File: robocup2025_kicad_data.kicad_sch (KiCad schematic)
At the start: 13 parts, among them M7 Motor_Servo, U2 ESP32-DEVKITC-32E

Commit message: added switch
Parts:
- added S1: tactile switch, robo:tactile switch, symbol robo:tactile switch
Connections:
- net ESP32_3.3: now also S1.2
- net ESP32_21: now reaches U2.J3_6 (IO21)
- net ESP32_21: now also S1.1
- no-connect marks 25 -> 24

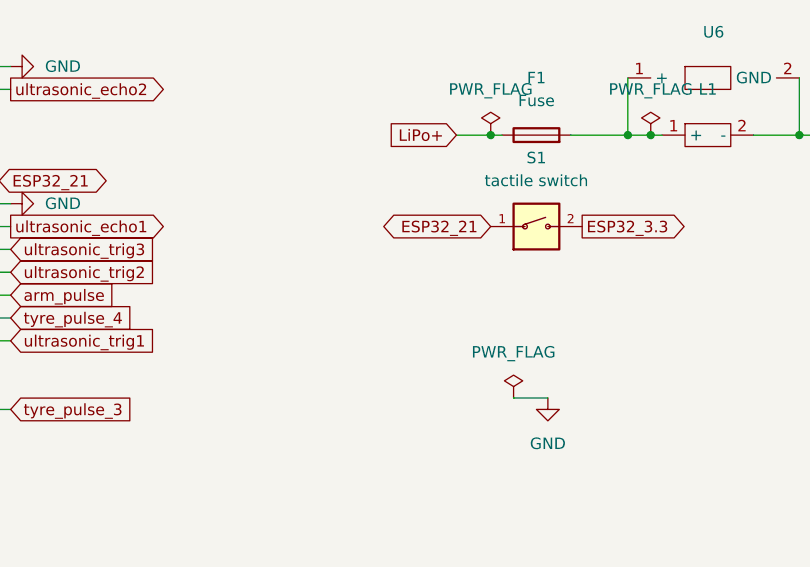
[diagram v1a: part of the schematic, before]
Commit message: fix: Made the pin "non-floating"
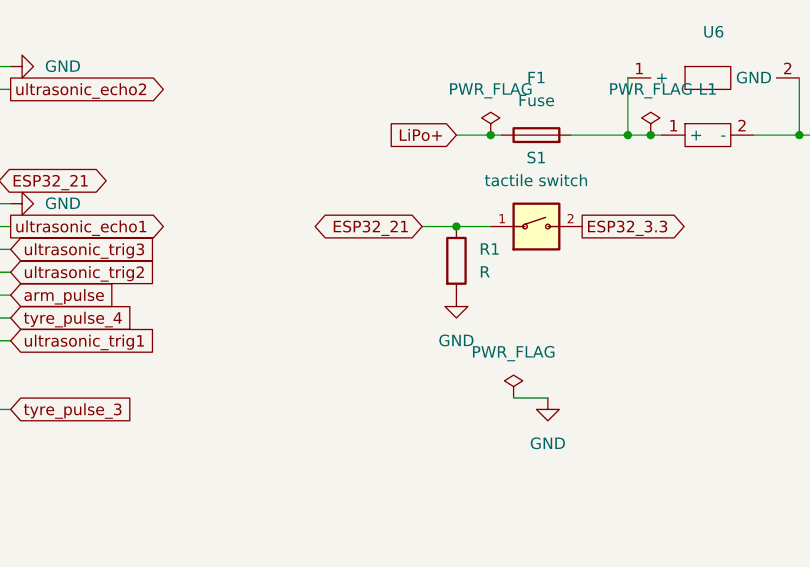
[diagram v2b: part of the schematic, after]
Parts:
- added R1: R, symbol Device:R
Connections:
- net ESP32_21: now also R1.1
- net GND: now also R1.2
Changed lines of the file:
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@@
 	)
 	(junction
+		(at 135.89 48.26)
+		(diameter 0)
+		(color 0 0 0 0)
+	)
+	(junction
 		(at 157.48 38.1)
 		(diameter 0)
@@
 	(wire
 		(pts
+			(xy 135.89 48.26) (xy 139.7 48.26)
+		)
+		(stroke
+			(width 0)
+			(type default)
+		)
+	)
+	(wire
+		(pts
 			(xy 82.55 55.88) (xy 86.36 55.88)
 		)
@@
 	(wire
 		(pts
+			(xy 132.08 48.26) (xy 135.89 48.26)
+		)
+		(stroke
+			(width 0)
+			(type default)
+		)
+	)
+	(wire
+		(pts
 			(xy 133.35 120.65) (xy 133.35 124.46)
 		)
@@
 	(global_label "ESP32_21"
 		(shape bidirectional)
-		(at 139.7 48.26 180)
+		(at 132.08 48.26 180)
 		(fields_autoplaced yes)
 		(effects
@@
 		)
 		(property "Intersheetrefs" "${INTERSHEET_REFS}"
-			(at 126.1694 48.26 0)
+			(at 118.5494 48.26 0)
 			(effects
 				(font
@@
 	)
 	(symbol
+		(lib_id "power:GND")
+		(at 135.89 55.88 0)
+		(unit 1)
+		(exclude_from_sim no)
+		(in_bom yes)
+		(on_board yes)
+		(dnp no)
+		(fields_autoplaced yes)
+		(property "Reference" "#PWR05"
+			(at 135.89 62.23 0)
+			(effects
+				(font
+					(size 1.27 1.27)
+				)
+				(hide yes)
+			)
+		)
+		(property "Value" "GND"
+			(at 135.89 60.96 0)
+			(effects
+				(font
+					(size 1.27 1.27)
+				)
+			)
+		)
+		(property "Footprint" ""
+			(at 135.89 55.88 0)
+			(effects
+				(font
+					(size 1.27 1.27)
+				)
+				(hide yes)
+			)
+		)
+		(property "Datasheet" ""
+			(at 135.89 55.88 0)
+			(effects
+				(font
+					(size 1.27 1.27)
+				)
+				(hide yes)
+			)
+		)
+		(property "Description" "Power symbol creates a global label with name \"GND\" , ground"
+			(at 135.89 55.88 0)
+			(effects
+				(font
+					(size 1.27 1.27)
+				)
+				(hide yes)
+			)
+		)
+		(pin "1"
+		)
+		(instances
+			(project ""
+				(path "/c41ae4e6-c818-4751-9662-d6273ae109e5"
+					(reference "#PWR05")
+					(unit 1)
+				)
+			)
+		)
+	)
+	(symbol
 		(lib_id "power:PWR_FLAG")
 		(at 139.7 38.1 0)
@@
 					(unit 1)
 				)
+			)
+		)
+	)
+	(symbol
+		(lib_id "Device:R")
+		(at 135.89 52.07 0)
+		(unit 1)
+		(exclude_from_sim no)
+		(in_bom yes)
+		(on_board yes)
+		(dnp no)
+		(fields_autoplaced yes)
+		(property "Reference" "R1"
+			(at 138.43 50.7999 0)
+			(effects
+				(font
+					(size 1.27 1.27)
+				)
+				(justify left)
+			)
+		)
+		(property "Value" "R"
+			(at 138.43 53.3399 0)
+			(effects
+				(font
+					(size 1.27 1.27)
+				)
+				(justify left)
+			)
+		)
+		(property "Footprint" ""
+			(at 134.112 52.07 90)
+			(effects
+				(font
+					(size 1.27 1.27)
+				)
+				(hide yes)
+			)
+		)
+		(property "Datasheet" "~"
+			(at 135.89 52.07 0)
+			(effects
+				(font
+					(size 1.27 1.27)
+				)
+				(hide yes)
+			)
+		)
+		(property "Description" "Resistor"
+			(at 135.89 52.07 0)
+			(effects
+				(font
+					(size 1.27 1.27)
+				)
+				(hide yes)
+			)
+		)
+		(pin "2"
+		)
+		(pin "1"
+		)
+		(instances
+			(project ""
+				(path "/c41ae4e6-c818-4751-9662-d6273ae109e5"
+					(reference "R1")
+					(unit 1)
+				)

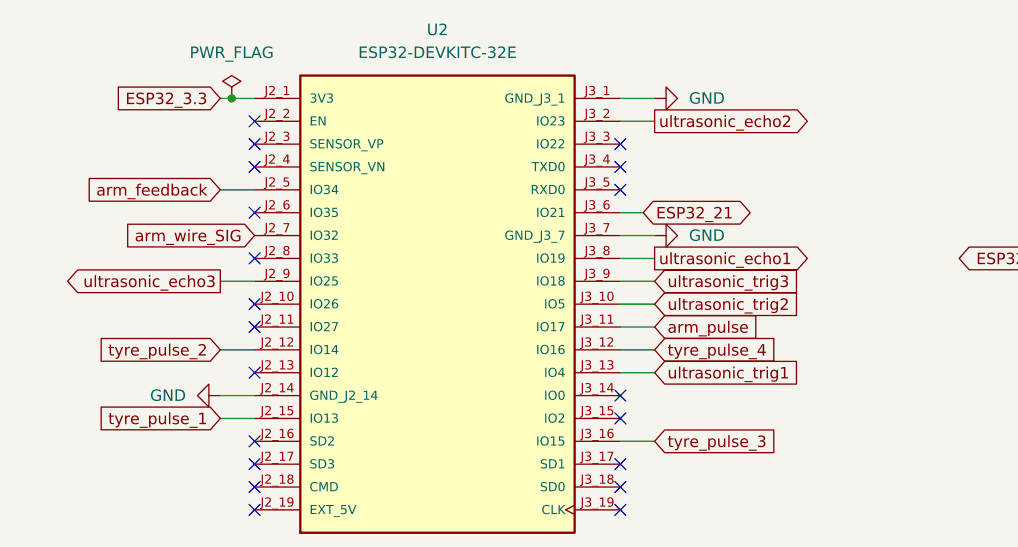
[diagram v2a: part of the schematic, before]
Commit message: Fix sch data
Edit ultra sonic's pin
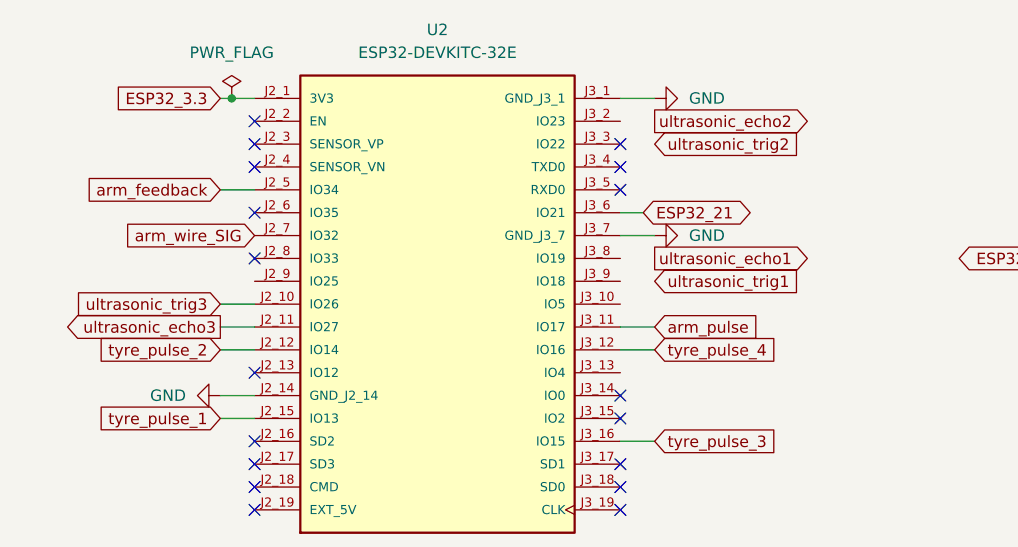
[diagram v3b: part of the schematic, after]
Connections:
- net ultrasonic_echo1: no longer U2.J3_8 (IO19)
- net ultrasonic_echo2: no longer U2.J3_2 (IO23)
- net ultrasonic_echo3: now also U2.J2_11 (IO27); no longer U2.J2_9 (IO25)
- net ultrasonic_trig1: no longer U2.J3_13 (IO4)
- net ultrasonic_trig2: no longer U2.J3_10 (IO5)
- net ultrasonic_trig3: now also U2.J2_10 (IO26); no longer U2.J3_9 (IO18)
- no-connect marks 24 -> 22
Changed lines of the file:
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@@
-	)
-	(no_connect
-		(at 41.91 53.34)
 	)
 	(no_connect
@@
 		(at 82.55 38.1)
 	)
-	(no_connect
-		(at 41.91 55.88)
-	)
 	(wire
 		(pts
@@
 	(wire
 		(pts
+			(xy 82.55 58.42) (xy 86.36 58.42)
+		)
+		(stroke
+			(width 0)
+			(type default)
+		)
+	)
+	(wire
+		(pts
 			(xy 135.89 48.26) (xy 139.7 48.26)
 		)
@@
 	(wire
 		(pts
-			(xy 82.55 53.34) (xy 86.36 53.34)
-		)
-		(stroke
-			(width 0)
-			(type default)
-		)
-	)
-	(wire
-		(pts
 			(xy 132.08 120.65) (xy 132.08 124.46)
 		)
@@
 	(wire
 		(pts
+			(xy 38.1 55.88) (xy 41.91 55.88)
+		)
+		(stroke
+			(width 0)
+			(type default)
+		)
+	)
+	(wire
+		(pts
 			(xy 114.3 120.65) (xy 114.3 124.46)
 		)
@@
 	(wire
 		(pts
-			(xy 82.55 33.02) (xy 86.36 33.02)
-		)
-		(stroke
-			(width 0)
-			(type default)
-		)
-	)
-	(wire
-		(pts
 			(xy 64.77 121.92) (xy 64.77 125.73)
 		)
@@
 	(wire
 		(pts
-			(xy 82.55 48.26) (xy 86.36 48.26)
-		)
-		(stroke
-			(width 0)
-			(type default)
-		)
-	)
-	(wire
-		(pts
 			(xy 125.73 120.65) (xy 125.73 124.46)
 		)
@@
 	(wire
 		(pts
+			(xy 38.1 53.34) (xy 41.91 53.34)
+		)
+		(stroke
+			(width 0)
+			(type default)
+		)
+	)
+	(wire
+		(pts
 			(xy 124.46 120.65) (xy 124.46 124.46)
 		)
@@
 	(wire
 		(pts
-			(xy 82.55 50.8) (xy 86.36 50.8)
-		)
-		(stroke
-			(width 0)
-			(type default)
-		)
-	)
-	(wire
-		(pts
 			(xy 146.05 67.31) (xy 142.24 67.31)
 		)
@@
 	(wire
 		(pts
-			(xy 82.55 60.96) (xy 86.36 60.96)
-		)
-		(stroke
-			(width 0)
-			(type default)
-		)
-	)
-	(wire
-		(pts
 			(xy 38.1 66.04) (xy 41.91 66.04)
 		)
@@
 	(wire
 		(pts
-			(xy 38.1 50.8) (xy 41.91 50.8)
-		)
-		(stroke
-			(width 0)
-			(type default)
-		)
-	)
-	(wire
-		(pts
 			(xy 82.55 68.58) (xy 86.36 68.58)
 		)
@@
 	(wire
 		(pts
-			(xy 82.55 58.42) (xy 86.36 58.42)
-		)
-		(stroke
-			(width 0)
-			(type default)
-		)
-	)
-	(wire
-		(pts
 			(xy 154.94 38.1) (xy 157.48 38.1)
 		)
@@
 	(global_label "ultrasonic_echo3"
 		(shape output)
-		(at 38.1 50.8 180)
-		(fields_autoplaced yes)
-		(effects
-			(font
-				(size 1.27 1.27)
-			)
-			(justify right)
-		)
-		(property "Intersheetrefs" "${INTERSHEET_REFS}"
-			(at 18.9679 50.8 0)
+		(at 38.1 55.88 180)
+		(fields_autoplaced yes)
+		(effects
+			(font
+				(size 1.27 1.27)
+			)
+			(justify right)
+		)
+		(property "Intersheetrefs" "${INTERSHEET_REFS}"
+			(at 18.9679 55.88 0)
 			(effects
 				(font
@@
 	(global_label "ultrasonic_trig1"
 		(shape input)
-		(at 86.36 60.96 0)
+		(at 86.36 50.8 0)
 		(fields_autoplaced yes)
 		(effects
@@
 		)
 		(property "Intersheetrefs" "${INTERSHEET_REFS}"
-			(at 104.2826 60.96 0)
+			(at 104.2826 50.8 0)
 			(effects
 				(font
@@
 	(global_label "ultrasonic_trig2"
 		(shape input)
-		(at 86.36 53.34 0)
+		(at 86.36 35.56 0)
 		(fields_autoplaced yes)
 		(effects
@@
 		)
 		(property "Intersheetrefs" "${INTERSHEET_REFS}"
-			(at 104.2826 53.34 0)
+			(at 104.2826 35.56 0)
 			(effects
 				(font
@@
 	(global_label "ultrasonic_trig3"
 		(shape input)
-		(at 86.36 50.8 0)
-		(fields_autoplaced yes)
-		(effects
-			(font
-				(size 1.27 1.27)
-			)
-			(justify left)
-		)
-		(property "Intersheetrefs" "${INTERSHEET_REFS}"
-			(at 104.2826 50.8 0)
-			(effects
-				(font
-					(size 1.27 1.27)
-				)
-				(justify left)
-				(hide yes)
-			)
+		(at 38.1 53.34 180)
+		(fields_autoplaced yes)
+		(effects
+			(font
+				(size 1.27 1.27)
+			)
+			(justify right)
+		)
+		(property "Intersheetrefs" "${INTERSHEET_REFS}"
+			(at 20.1774 53.34 0)
+			(effects
+				(font
+					(size 1.27 1.27)
+				)
+				(justify right)
+				(hide yes)
+			)

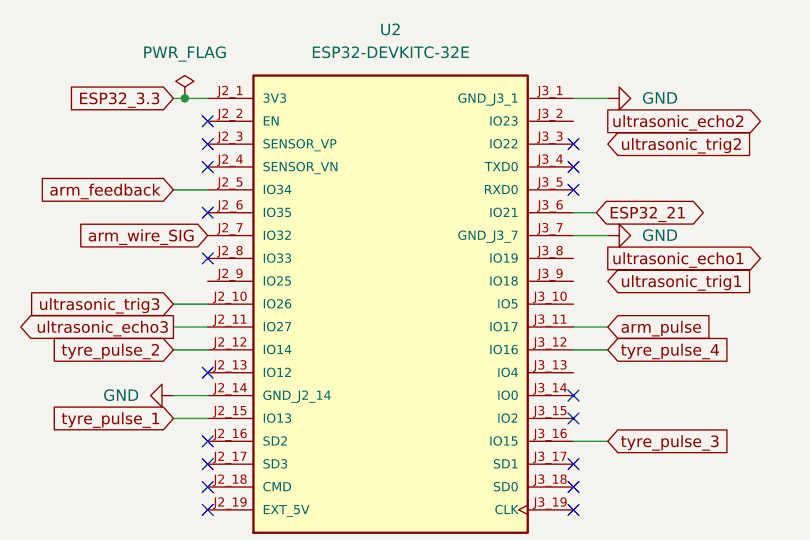
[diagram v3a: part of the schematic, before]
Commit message: updated schematics
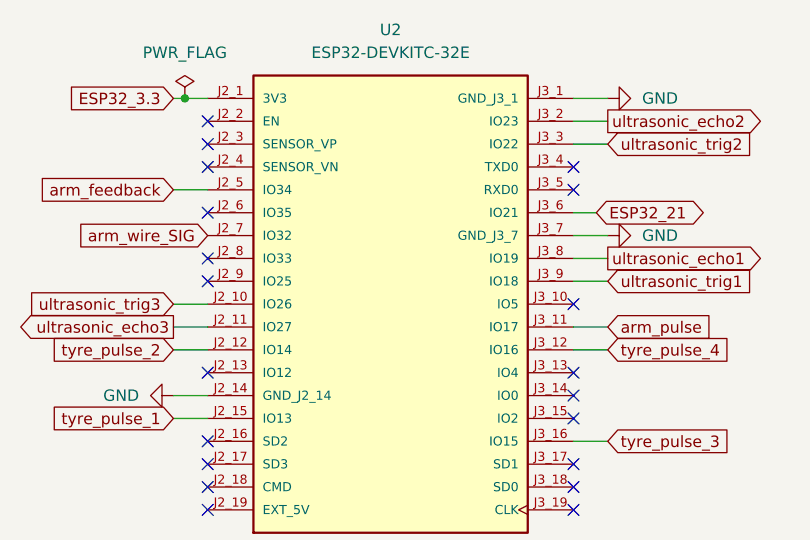
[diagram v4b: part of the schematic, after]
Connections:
- net ultrasonic_echo1: now also U2.J3_8 (IO19)
- net ultrasonic_echo2: now also U2.J3_2 (IO23)
- net ultrasonic_trig1: now also U2.J3_9 (IO18)
- net ultrasonic_trig2: now also U2.J3_3 (IO22)
- no-connect marks 22 -> 24
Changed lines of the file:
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@@
-	)
-	(no_connect
-		(at 82.55 35.56)
 	)
 	(no_connect
@@
 	)
 	(no_connect
+		(at 82.55 60.96)
+	)
+	(no_connect
 		(at 41.91 121.92)
 	)
@@
 	)
 	(no_connect
+		(at 82.55 53.34)
+	)
+	(no_connect
 		(at 41.91 35.56)
 	)
@@
 	)
 	(no_connect
+		(at 41.91 50.8)
+	)
+	(no_connect
 		(at 54.61 121.92)
 	)
@@
 	(wire
 		(pts
+			(xy 82.55 50.8) (xy 86.36 50.8)
+		)
+		(stroke
+			(width 0)
+			(type default)
+		)
+	)
+	(wire
+		(pts
+			(xy 82.55 48.26) (xy 86.36 48.26)
+		)
+		(stroke
+			(width 0)
+			(type default)
+		)
+	)
+	(wire
+		(pts
 			(xy 38.1 58.42) (xy 41.91 58.42)
 		)
@@
 	(wire
 		(pts
+			(xy 82.55 35.56) (xy 86.36 35.56)
+		)
+		(stroke
+			(width 0)
+			(type default)
+		)
+	)
+	(wire
+		(pts
 			(xy 38.1 53.34) (xy 41.91 53.34)
 		)
@@
 		)
 		(stroke
+			(width 0)
+			(type default)
+		)
+	)
+	(wire
+		(pts
+			(xy 82.55 33.02) (xy 86.36 33.02)
+		)
+		(stroke

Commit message: updated sch
assigned footprint for resistor
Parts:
- R1: footprint (none) -> Resistor_THT:R_Axial_DIN0204_L3.6mm_D1.6mm_P7.62mm_Horizontal
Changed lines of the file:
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@@
 			)
 		)
-		(property "Footprint" ""
+		(property "Footprint" "Resistor_THT:R_Axial_DIN0204_L3.6mm_D1.6mm_P7.62mm_Horizontal"
 			(at 134.112 52.07 90)
 			(effects

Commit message: new edge on pcb
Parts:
- S1: footprint robo:tactile switch -> robo:DS-850K-S-ON
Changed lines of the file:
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@@
 			)
 		)
-		(property "Footprint" "robo:tactile switch"
+		(property "Footprint" "robo:DS-850K-S-ON"
 			(at 144.78 48.26 0)
 			(effects

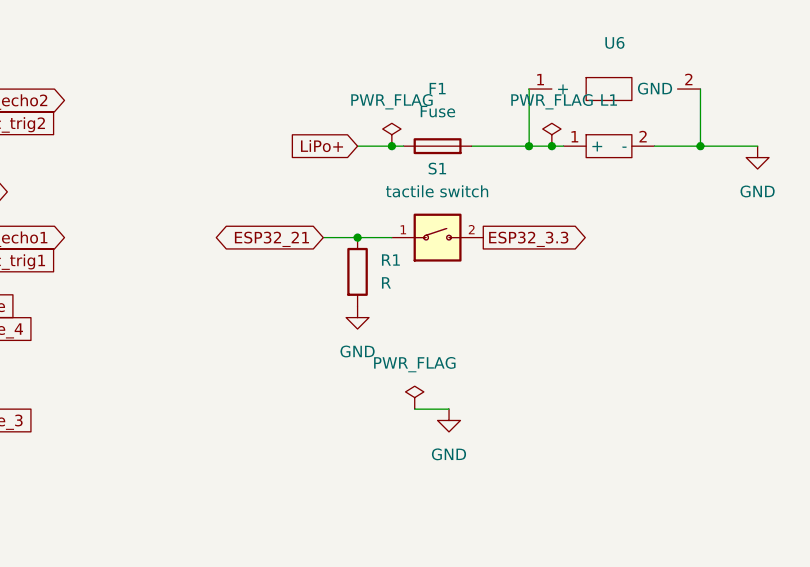
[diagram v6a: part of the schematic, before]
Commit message: Added value of resistor
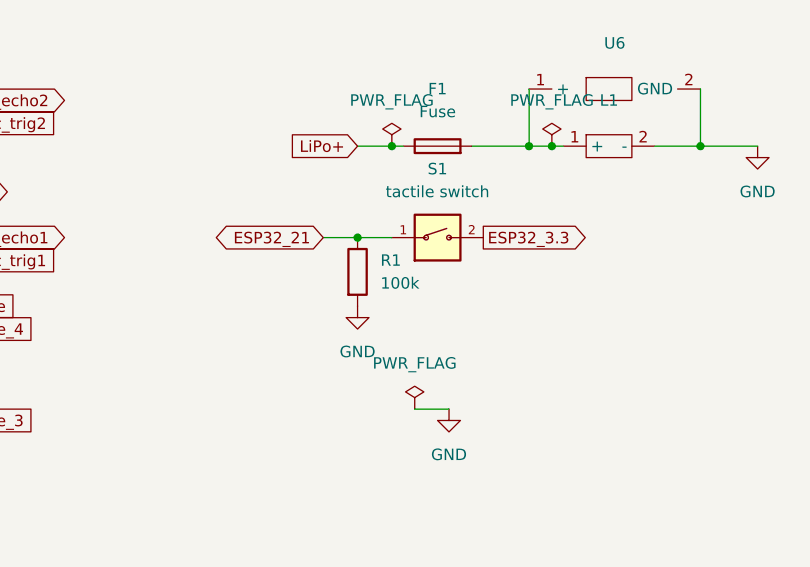
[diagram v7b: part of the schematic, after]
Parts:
- R1: value R -> 100k
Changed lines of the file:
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@@
 			)
 		)
-		(property "Value" "R"
+		(property "Value" "100k"
 			(at 138.43 53.3399 0)
 			(effects
